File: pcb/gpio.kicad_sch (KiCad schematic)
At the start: 18 parts, among them J5 Conn_01x04, J6 PJ-242D-SMT, J7 PJ-242D-SMT, U6 EL357, U7 EL357

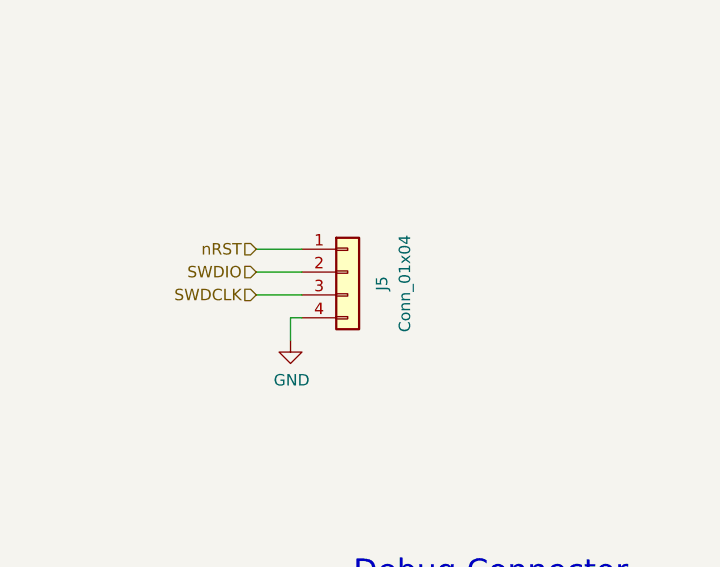
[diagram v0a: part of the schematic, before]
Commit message: Add datasheet links
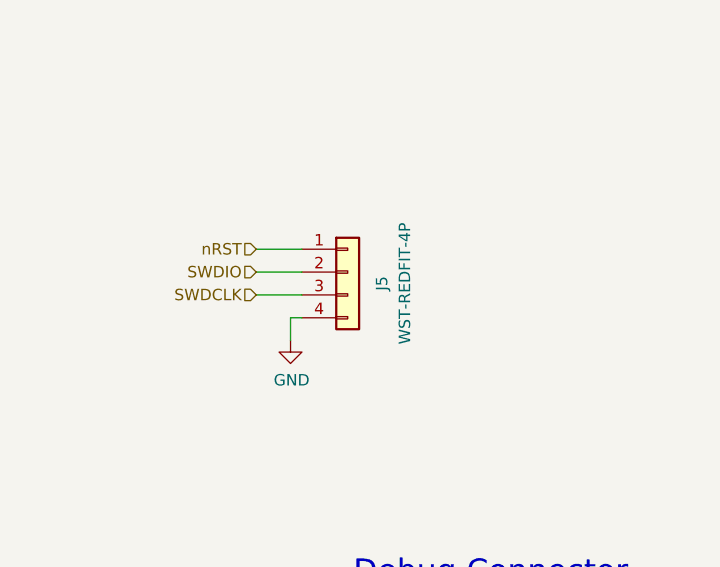
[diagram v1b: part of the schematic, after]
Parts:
- J5: value Conn_01x04 -> WST-REDFIT-4P
- U6, U7: Manufacturer Part Number EL357N(B)(TA)-G -> EL357N(B)(TA)-G
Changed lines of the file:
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@@
       (effects (font (size 1.27 1.27)) hide)
     )
-    (property "Datasheet" "~" (id 3) (at 233.68 129.54 0)
+    (property "Datasheet" "https://datasheet.lcsc.com/lcsc/1811061026_Everlight-Elec-19-237-R6GHBHC-A07-2T_C264511.pdf" (id 3) (at 233.68 129.54 0)
       (effects (font (size 1.27 1.27)) hide)
     )
@@
       (effects (font (size 1.27 1.27)) hide)
     )
-    (property "Datasheet" "" (id 3) (at 73.66 165.1 0)
+    (property "Datasheet" "https://datasheet.lcsc.com/lcsc/1809192312_Everlight-Elec-EL357N-B-TA-G_C6649.pdf" (id 3) (at 73.66 165.1 0)
       (effects (font (size 1.27 1.27)) hide)
     )
@@
       (effects (font (size 1.27 1.27)) hide)
     )
-    (property "Manufacturer Part Number" " EL357N(B)(TA)-G" (id 5) (at 73.66 165.1 0)
+    (property "Manufacturer Part Number" "EL357N(B)(TA)-G" (id 5) (at 73.66 165.1 0)
       (effects (font (size 1.27 1.27)) hide)
     )
@@
     (in_bom yes) (on_board yes) (fields_autoplaced)
     (property "Reference" "J5" (id 0) (at 251.46 52.705 90))
-    (property "Value" "Conn_01x04" (id 1) (at 254 52.705 90))
+    (property "Value" "WST-REDFIT-4P" (id 1) (at 254 52.705 90))
     (property "Footprint" "ultramote:WR_WST-REDFIT-4P_DEBUG" (id 2) (at 247.65 51.435 0)
       (effects (font (size 1.27 1.27)) hide)
     )
-    (property "Datasheet" "~" (id 3) (at 247.65 51.435 0)
+    (property "Datasheet" "https://www.we-online.com/components/products/datasheet/490107670412.pdf" (id 3) (at 247.65 51.435 0)
       (effects (font (size 1.27 1.27)) hide)
     )
@@
       (effects (font (size 1.27 1.27)) hide)
     )
-    (property "Datasheet" "~" (id 3) (at 38.735 54.61 0)
+    (property "Datasheet" "https://datasheet.lcsc.com/lcsc/2110151630_XKB-Connectivity-PJ-242D-SMT_C381133.pdf" (id 3) (at 38.735 54.61 0)
       (effects (font (size 1.27 1.27)) hide)
     )
@@
       (effects (font (size 1.27 1.27)) hide)
     )
-    (property "Datasheet" "~" (id 3) (at 52.07 148.59 0)
+    (property "Datasheet" "https://datasheet.lcsc.com/lcsc/2110151630_XKB-Connectivity-PJ-242D-SMT_C381133.pdf" (id 3) (at 52.07 148.59 0)
       (effects (font (size 1.27 1.27)) hide)
     )
@@
       (effects (font (size 1.27 1.27)) hide)
     )
-    (property "Datasheet" "" (id 3) (at 73.66 151.13 0)
+    (property "Datasheet" "https://datasheet.lcsc.com/lcsc/1809192312_Everlight-Elec-EL357N-B-TA-G_C6649.pdf" (id 3) (at 73.66 151.13 0)
       (effects (font (size 1.27 1.27)) hide)
     )
@@
       (effects (font (size 1.27 1.27)) hide)
     )
-    (property "Manufacturer Part Number" " EL357N(B)(TA)-G" (id 5) (at 73.66 151.13 0)
-      (effects (font (size 1.27 1.27)) hide)
-    )
+    (property "Manufacturer Part Number" "EL357N(B)(TA)-G" (id 5) (at 73.66 151.13 0)
+      (effects (font (size 1.27 1.27)) hide)
+    )

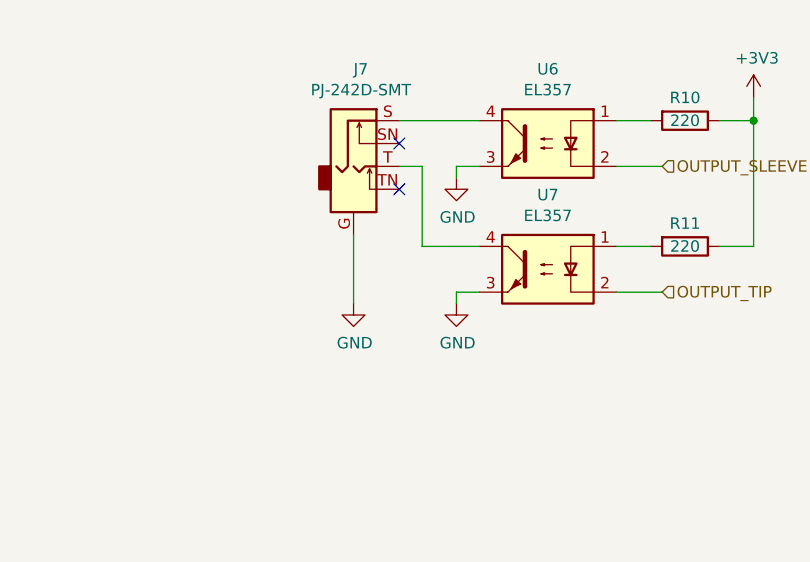
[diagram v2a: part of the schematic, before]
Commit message: Route Output jack through separate ground
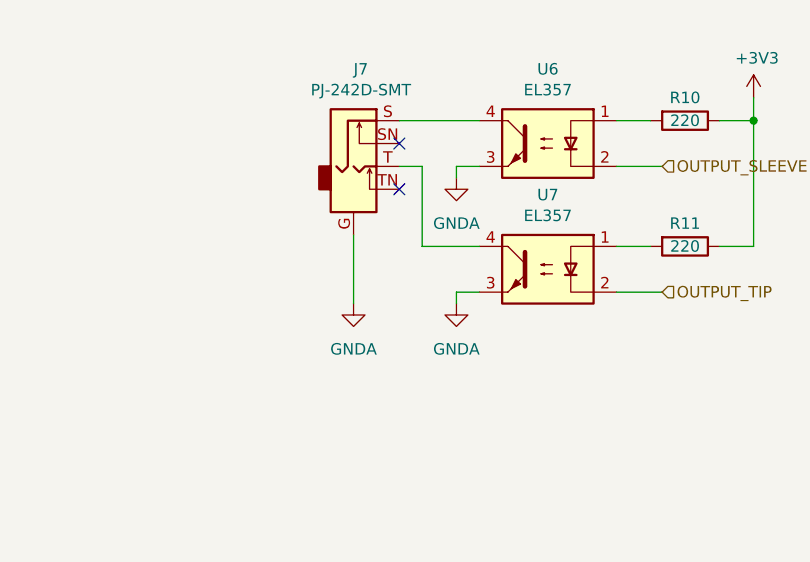
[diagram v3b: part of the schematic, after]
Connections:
- net GND: no longer J7.G, U6.3, U7.3
- new net GNDA: J7.G, U6.3, U7.3
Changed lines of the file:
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@@
 (kicad_sch (version 20230121) (generator eeschema)
   (paper "A4")
+  (title_block
+    (date "2023-06-19")
+    (rev "v0.3")
+  )
   (junction (at 80.01 80.01) (diameter 0) (color 0 0 0 0)
   )
@@
     )
   )
-  (symbol (lib_id "power:GND") (at 63.5 154.94 0) (unit 1)
-    (in_bom yes) (on_board yes) (dnp no)
-    (property "Reference" "#PWR044" (at 63.5 161.29 0)
-      (effects (font (size 1.27 1.27)) hide)
-    )
-    (property "Value" "GND" (at 63.627 159.3342 0)
+  (symbol (lib_id "power:GNDA") (at 63.5 154.94 0) (unit 1)
+    (in_bom yes) (on_board yes) (dnp no) (fields_autoplaced)
+    (property "Reference" "#PWR045" (at 63.5 161.29 0)
+      (effects (font (size 1.27 1.27)) hide)
+    )
+    (property "Value" "GNDA" (at 63.5 160.02 0)
       (effects (font (size 1.27 1.27)))
     )
@@
       (project "ultramote"
         (path "/d9165d03-bf8e-4912-9bca-224da4ea4a29/43fad132-fb74-49a6-968f-ee47e7e9e12e"
-          (reference "#PWR044") (unit 1)
+          (reference "#PWR045") (unit 1)
         )
       )
@@
     )
   )
-  (symbol (lib_id "power:GND") (at 52.07 168.91 0) (unit 1)
-    (in_bom yes) (on_board yes) (dnp no)
-    (property "Reference" "#PWR043" (at 52.07 175.26 0)
-      (effects (font (size 1.27 1.27)) hide)
-    )
-    (property "Value" "GND" (at 52.197 173.3042 0)
-      (effects (font (size 1.27 1.27)))
-    )
-    (property "Footprint" "" (at 52.07 168.91 0)
-      (effects (font (size 1.27 1.27)) hide)
-    )
-    (property "Datasheet" "" (at 52.07 168.91 0)
+  (symbol (lib_id "Device:R") (at 254 123.19 270) (unit 1)
+    (in_bom yes) (on_board yes) (dnp no)
+    (property "Reference" "R16" (at 254 120.65 90)
+      (effects (font (size 1.27 1.27)))
+    )
+    (property "Value" "220" (at 254 123.19 90)
+      (effects (font (size 1.27 1.27)))
+    )
+    (property "Footprint" "Resistor_SMD:R_0603_1608Metric" (at 254 121.412 90)
+      (effects (font (size 1.27 1.27)) hide)
+    )
+    (property "Datasheet" "~" (at 254 123.19 0)
+      (effects (font (size 1.27 1.27)) hide)
+    )
+    (property "LCSC Part Number" "C22962" (at 254 123.19 0)
+      (effects (font (size 1.27 1.27)) hide)
+    )
+    (property "Manufacturer Part Number" "0603WAF2200T5E" (at 254 123.19 0)
+      (effects (font (size 1.27 1.27)) hide)
+    )
+    (pin "1")
+    (pin "2")
+    (instances
+      (project "ultramote"
+        (path "/d9165d03-bf8e-4912-9bca-224da4ea4a29/43fad132-fb74-49a6-968f-ee47e7e9e12e"
+          (reference "R16") (unit 1)
+        )
+      )
+    )
+  )
+  (symbol (lib_id "Device:R") (at 88.9 148.59 270) (unit 1)
+    (in_bom yes) (on_board yes) (dnp no)
+    (property "Reference" "R10" (at 88.9 146.05 90)
+      (effects (font (size 1.27 1.27)))
+    )
+    (property "Value" "220" (at 88.9 148.59 90)
+      (effects (font (size 1.27 1.27)))
+    )
+    (property "Footprint" "Resistor_SMD:R_0603_1608Metric" (at 88.9 146.812 90)
+      (effects (font (size 1.27 1.27)) hide)
+    )
+    (property "Datasheet" "~" (at 88.9 148.59 0)
+      (effects (font (size 1.27 1.27)) hide)
+    )
+    (property "LCSC Part Number" "C22962" (at 88.9 148.59 0)
+      (effects (font (size 1.27 1.27)) hide)
+    )
+    (property "Manufacturer Part Number" "0603WAF2200T5E" (at 88.9 148.59 0)
+      (effects (font (size 1.27 1.27)) hide)
+    )
+    (pin "1")
+    (pin "2")
+    (instances
+      (project "ultramote"
+        (path "/d9165d03-bf8e-4912-9bca-224da4ea4a29/43fad132-fb74-49a6-968f-ee47e7e9e12e"
+          (reference "R10") (unit 1)
+        )
+      )
+    )
+  )
+  (symbol (lib_id "power:GNDA") (at 63.5 168.91 0) (unit 1)
+    (in_bom yes) (on_board yes) (dnp no) (fields_autoplaced)
+    (property "Reference" "#PWR043" (at 63.5 175.26 0)
+      (effects (font (size 1.27 1.27)) hide)
+    )
+    (property "Value" "GNDA" (at 63.5 173.99 0)
+      (effects (font (size 1.27 1.27)))
+    )
+    (property "Footprint" "" (at 63.5 168.91 0)
+      (effects (font (size 1.27 1.27)) hide)
+    )
+    (property "Datasheet" "" (at 63.5 168.91 0)
       (effects (font (size 1.27 1.27)) hide)
     )
@@
         (path "/d9165d03-bf8e-4912-9bca-224da4ea4a29/43fad132-fb74-49a6-968f-ee47e7e9e12e"
           (reference "#PWR043") (unit 1)
-        )
-      )
-    )
-  )
-  (symbol (lib_id "Device:R") (at 254 123.19 270) (unit 1)
-    (in_bom yes) (on_board yes) (dnp no)
-    (property "Reference" "R16" (at 254 120.65 90)
-      (effects (font (size 1.27 1.27)))
-    )
-    (property "Value" "220" (at 254 123.19 90)
-      (effects (font (size 1.27 1.27)))
-    )
-    (property "Footprint" "Resistor_SMD:R_0603_1608Metric" (at 254 121.412 90)
-      (effects (font (size 1.27 1.27)) hide)
-    )
-    (property "Datasheet" "~" (at 254 123.19 0)
-      (effects (font (size 1.27 1.27)) hide)
-    )
-    (property "LCSC Part Number" "C22962" (at 254 123.19 0)
-      (effects (font (size 1.27 1.27)) hide)
-    )
-    (property "Manufacturer Part Number" "0603WAF2200T5E" (at 254 123.19 0)
-      (effects (font (size 1.27 1.27)) hide)
-    )
-    (pin "1")
-    (pin "2")
-    (instances
-      (project "ultramote"
-        (path "/d9165d03-bf8e-4912-9bca-224da4ea4a29/43fad132-fb74-49a6-968f-ee47e7e9e12e"
-          (reference "R16") (unit 1)
-        )
-      )
-    )
-  )
-  (symbol (lib_id "Device:R") (at 88.9 148.59 270) (unit 1)
-    (in_bom yes) (on_board yes) (dnp no)
-    (property "Reference" "R10" (at 88.9 146.05 90)
-      (effects (font (size 1.27 1.27)))
-    )
-    (property "Value" "220" (at 88.9 148.59 90)
-      (effects (font (size 1.27 1.27)))
-    )
-    (property "Footprint" "Resistor_SMD:R_0603_1608Metric" (at 88.9 146.812 90)
-      (effects (font (size 1.27 1.27)) hide)
-    )
-    (property "Datasheet" "~" (at 88.9 148.59 0)
-      (effects (font (size 1.27 1.27)) hide)
-    )
-    (property "LCSC Part Number" "C22962" (at 88.9 148.59 0)
-      (effects (font (size 1.27 1.27)) hide)
-    )
-    (property "Manufacturer Part Number" "0603WAF2200T5E" (at 88.9 148.59 0)
-      (effects (font (size 1.27 1.27)) hide)
-    )
-    (pin "1")
-    (pin "2")
-    (instances
-      (project "ultramote"
-        (path "/d9165d03-bf8e-4912-9bca-224da4ea4a29/43fad132-fb74-49a6-968f-ee47e7e9e12e"
-          (reference "R10") (unit 1)
         )
       )
@@
     )
   )
-  (symbol (lib_id "power:GND") (at 63.5 168.91 0) (unit 1)
-    (in_bom yes) (on_board yes) (dnp no)
-    (property "Reference" "#PWR045" (at 63.5 175.26 0)
-      (effects (font (size 1.27 1.27)) hide)
-    )
-    (property "Value" "GND" (at 63.627 173.3042 0)
-      (effects (font (size 1.27 1.27)))
-    )
-    (property "Footprint" "" (at 63.5 168.91 0)
-      (effects (font (size 1.27 1.27)) hide)
-    )
-    (property "Datasheet" "" (at 63.5 168.91 0)
-      (effects (font (size 1.27 1.27)) hide)
-    )
-    (pin "1")
-    (instances
-      (project "ultramote"
-        (path "/d9165d03-bf8e-4912-9bca-224da4ea4a29/43fad132-fb74-49a6-968f-ee47e7e9e12e"
-          (reference "#PWR045") (unit 1)
-        )
-      )
-    )
-  )
   (symbol (lib_id "power:+3V3") (at 96.52 146.05 0) (unit 1)
     (in_bom yes) (on_board yes) (dnp no)
@@
         )
       )
+    )
+  )
+  (symbol (lib_id "power:GNDA") (at 52.07 168.91 0) (unit 1)
+    (in_bom yes) (on_board yes) (dnp no) (fields_autoplaced)
+    (property "Reference" "#PWR028" (at 52.07 175.26 0)
+      (effects (font (size 1.27 1.27)) hide)
+    )
+    (property "Value" "GNDA" (at 52.07 173.99 0)
+      (effects (font (size 1.27 1.27)))
+    )
+    (property "Footprint" "" (at 52.07 168.91 0)
+      (effects (font (size 1.27 1.27)) hide)
+    )
+    (property "Datasheet" "" (at 52.07 168.91 0)
+      (effects (font (size 1.27 1.27)) hide)
+    )
+    (pin "1")
+    (instances
+      (project "ultramote"
+        (path "/d9165d03-bf8e-4912-9bca-224da4ea4a29/43fad132-fb74-49a6-968f-ee47e7e9e12e"
+          (reference "#PWR028") (unit 1)
+        )
+      )
